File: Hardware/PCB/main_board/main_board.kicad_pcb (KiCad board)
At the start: 2 copper layers, 150 x 160 mm, 99 parts, among them J1 SWD, J2 USB_A, J3 DIN-5_180degree, J4 USB_B, J5 Conn_Coaxial, J6 AudioJack3, Q1 BC547, U1 MCP6002-xSN, U2 NUCLEO-F446RE, U3 6N137, U4 RC4558

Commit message: Route PCB changes
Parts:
- added C33: 100n, Capacitor_SMD:C_0805_2012Metric, F.Cu at (108.8, 200.6)
- added C34: 100n, Capacitor_SMD:C_0805_2012Metric, F.Cu at (97.4, 107.5)
- added C35: 100n, Capacitor_SMD:C_0805_2012Metric, F.Cu at (94.0, 108.5)
- added C36: 47u, Capacitor_SMD:CP_Elec_6.3x5.4, F.Cu at (95.0, 100.0)
- added C37: 4.7u, Capacitor_SMD:C_0805_2012Metric, F.Cu at (85.0, 110.4)
- added C38: 150p, Capacitor_SMD:C_0805_2012Metric, F.Cu at (86.5, 114.0)
- added C39: 47u, Capacitor_SMD:CP_Elec_6.3x5.4, F.Cu at (95.0, 92.5)
- added Q2: BC847B, Package_TO_SOT_SMD:SOT-23, F.Cu at (84.0, 100.5)
- added Q3: BC847B, Package_TO_SOT_SMD:SOT-23, F.Cu at (88.0, 96.5)
- added Q4: BC857B, Package_TO_SOT_SMD:SOT-23, F.Cu at (88.0, 100.5)
- added Q5: BC847B, Package_TO_SOT_SMD:SOT-23, F.Cu at (89.0, 204.0)
- added R20: 3.9k, Resistor_SMD:R_0805_2012Metric, F.Cu at (104.4, 203.5)
- added R21: 10k, Resistor_SMD:R_0805_2012Metric, F.Cu at (108.1, 203.5)
- added R22: 22M, Resistor_SMD:R_0805_2012Metric, F.Cu at (97.4, 105.5)
- added R23: 10k, Resistor_SMD:R_0805_2012Metric, F.Cu at (97.4, 111.5)
- added R24: 10M, Resistor_SMD:R_0805_2012Metric, F.Cu at (97.4, 109.5)
- added R25: 10k, Resistor_SMD:R_0805_2012Metric, F.Cu at (97.4, 113.5)
- added R26: 1k, Resistor_SMD:R_0805_2012Metric, F.Cu at (94.0, 112.0)
- added R27: 33, Resistor_SMD:R_0805_2012Metric, F.Cu at (85.0, 106.6)
- added R28: 10k, Resistor_SMD:R_0805_2012Metric, F.Cu at (84.0, 93.0)
- added R29: 10k, Resistor_SMD:R_0805_2012Metric, F.Cu at (88.0, 103.5)
- added R30: 56k, Resistor_SMD:R_0805_2012Metric, F.Cu at (90.0, 114.0)
- added R31: 10k, Resistor_SMD:R_0805_2012Metric, F.Cu at (87.5, 89.0)
- added R32: 100, Resistor_SMD:R_0805_2012Metric, F.Cu at (87.5, 93.0)
- added R33: 100, Resistor_SMD:R_0805_2012Metric, F.Cu at (87.5, 91.0)
- added U5: MCP6002-xSN, Package_SO:SOIC-8_3.9x4.9mm_P1.27mm, F.Cu at (90.0, 108.5)
- Q1: value BC547 -> BC857B; footprint Package_TO_SOT_THT:TO-92_Inline -> Package_TO_SOT_SMD:SOT-23
- RV_VOL1: value R_POT_Dual -> 500k reverse log; footprint Potentiometer_THT:Potentiometer_Alps_RK09L_Double_Vertical -> Potentiometer_THT:Potentiometer_Alps_RK09K_Single_Vertical
- moved Q1 106.6 mm to (84.0, 96.5), turned to 180 degrees
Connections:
- C16 pad 2: /analogFX/OUT_VCF__IN_DIST -> /analogFX/IN_DIST
- C4 pad 1: /analogFX/OUT_VCF__IN_DIST -> /analogFX/OUT_VCF
- Q1 pad 1: Net-(C2-Pad1) -> Net-(Q1-Pad1)
- R1 pad 1: Net-(Q1-Pad2) -> Net-(Q5-Pad1)
- R19 pad 2: /analogFX/AUDIO_OUT -> /audio_out/AUDIO_IN
- R2 pad 1: Net-(Q1-Pad2) -> Net-(Q5-Pad1)
- R5 pad 1: Net-(R5-Pad1) -> /analogFX/2.5V_midpoint
- R6 pad 1: Net-(R5-Pad1) -> /analogFX/2.5V_midpoint
- RV_VOL1 pad 1: Net-(RV_VOL1-Pad1) -> Net-(C38-Pad2)
- RV_VOL1 pad 2: Net-(RV_VOL1-Pad2) -> Net-(C38-Pad2)
- U1 pad 3: Net-(R5-Pad1) -> /analogFX/2.5V_midpoint
- U1 pad 5: GND -> /analogFX/2.5V_midpoint
- U1 pad 6: Net-(U1-Pad6) -> Net-(R20-Pad1)
- U1 pad 7: Net-(U1-Pad6) -> Net-(C33-Pad2)
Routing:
- net +5VA: track 250.0 -> 356.7 mm, vias 0 -> 6
- net Net-(J6-PadR): track 5.50 -> 106.6 mm, vias 0 -> 2
- net /audio_out/AUDIO_IN: track 0.00 -> 99.0 mm, vias 0 -> 4
- net Net-(C38-Pad2): track 0.00 -> 46.3 mm, vias 0 -> 2
- net Net-(C38-Pad1): track 0.00 -> 42.1 mm, vias 0 -> 2
- net Net-(R27-Pad2): track 0.00 -> 38.1 mm, vias 0 -> 2
- net /analogFX/OUT_VCF__IN_DIST: track 34.2 -> 0.00 mm, vias 2 -> 0
- net GND: track 74.7 -> 107.3 mm, vias 10 -> 16
- net /analogFX/IN_DIST: track 0.00 -> 25.4 mm, vias 0 -> 2
- net Net-(C33-Pad2): track 0.00 -> 23.1 mm, vias 0 -> 2
- net Net-(Q5-Pad1): track 0.00 -> 20.6 mm
- net Net-(R20-Pad1): track 0.00 -> 20.5 mm, vias 0 -> 2
- net Net-(Q1-Pad1): track 0.00 -> 16.9 mm
- net Net-(Q1-Pad2): track 21.7 -> 7.08 mm
- net Net-(C36-Pad1): track 0.00 -> 14.3 mm
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
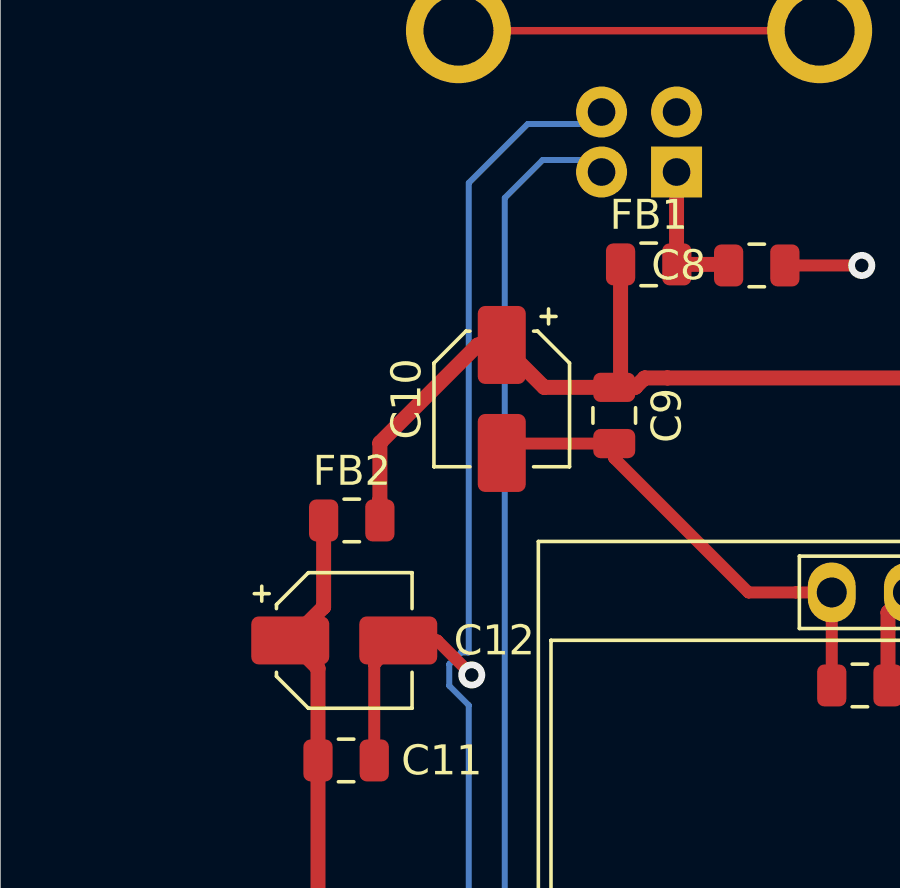
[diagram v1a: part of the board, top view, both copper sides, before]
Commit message: Fix GND via
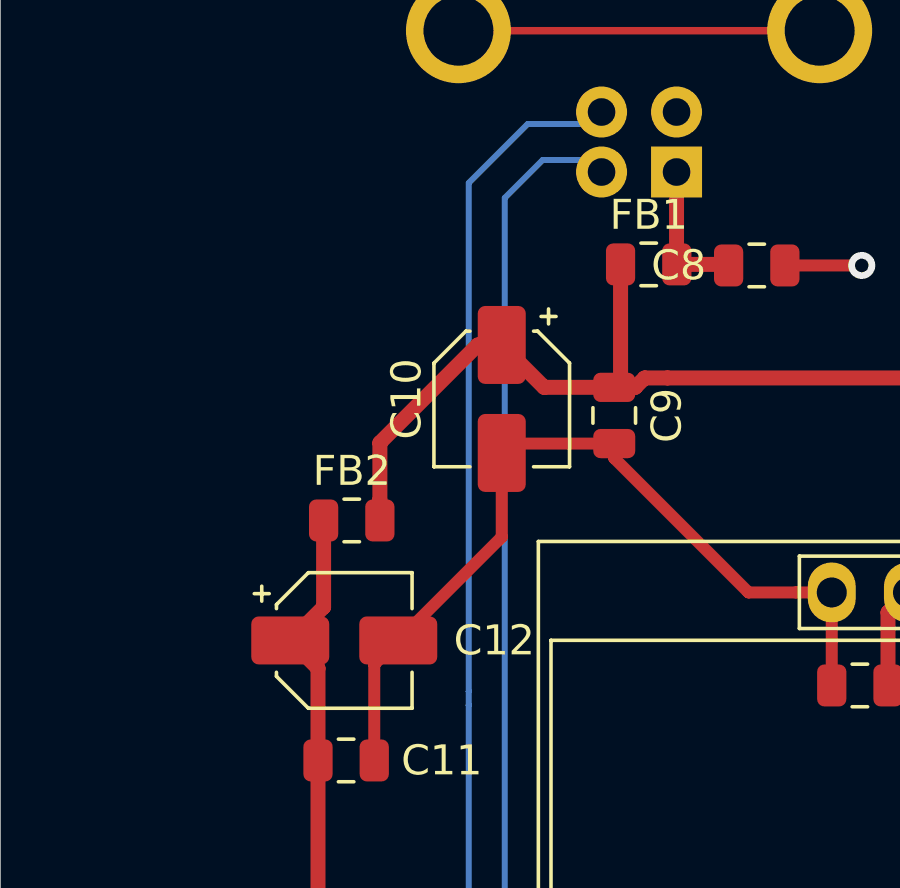
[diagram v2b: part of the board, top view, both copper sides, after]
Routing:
- net GND: track 107.3 -> 112.1 mm, vias 16 -> 15
- net /power/USB_B_D+: track 152.9 -> 152.2 mm
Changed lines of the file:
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@@
     (thickness 1.6)
     (drawings 3)
-    (tracks 945)
+    (tracks 942)
     (zones 0)
     (modules 125)
@@
   )
   (setup
-    (last_trace_width 0.5)
+    (last_trace_width 0.25)
     (user_trace_width 0.5)
     (trace_clearance 0.2)
@@
   (segment (start 85.85 95.55) (end 85.7 95.55) (width 0.25) (layer F.Cu) (net 6))
   (segment (start 87.1 97.5) (end 87.1 96.8) (width 0.25) (layer F.Cu) (net 6))
-  (segment (start 99.912 207.4835) (end 99.912 209.1645) (width 0.25) (layer F.Cu) (net 135))
   (segment (start 97.88 208.4025) (end 97.88 207.054) (width 0.4) (layer F.Cu) (net 7))
   (segment (start 110.983 79.386) (end 110.683 79.086) (width 0.4) (layer F.Cu) (net 7))
@@
   (segment (start 47.5 91.55) (end 48.3 90.75) (width 0.4) (layer F.Cu) (net 7))
   (segment (start 47.5 94.75) (end 47.5 91.55) (width 0.4) (layer F.Cu) (net 7))
-  (segment (start 49.6 90.75) (end 50.75 91.9) (width 0.4) (layer F.Cu) (net 7))
-  (segment (start 48.3 90.75) (end 49.6 90.75) (width 0.4) (layer F.Cu) (net 7))
-  (segment (start 50.75 91.9) (end 50.75 91.9) (width 0.4) (layer F.Cu) (net 7))
-  (via (at 50.75 91.9) (size 0.9) (drill 0.45) (layers F.Cu B.Cu) (net 7))
   (segment (start 89.75 74.0575) (end 87.3075 76.5) (width 0.4) (layer F.Cu) (net 7))
   (segment (start 89.75 72.96) (end 89.75 74.0575) (width 0.4) (layer F.Cu) (net 7))
@@
   (via (at 87 87.5) (size 0.9) (drill 0.45) (layers F.Cu B.Cu) (net 7))
   (segment (start 86.5625 87.9375) (end 87 87.5) (width 0.4) (layer F.Cu) (net 7))
+  (segment (start 51.75 87.3) (end 48.3 90.75) (width 0.4) (layer F.Cu) (net 7))
+  (segment (start 51.75 84.5) (end 51.75 87.3) (width 0.4) (layer F.Cu) (net 7))
   (segment (start 99.426473 211.525027) (end 99.912 211.0395) (width 0.25) (layer F.Cu) (net 8))
   (segment (start 92.7015 218.25) (end 99.426473 211.525027) (width 0.25) (layer F.Cu) (net 8))
   (segment (start 55.25 214.75) (end 58.75 218.25) (width 0.25) (layer F.Cu) (net 8))
   (segment (start 58.75 218.25) (end 92.7015 218.25) (width 0.25) (layer F.Cu) (net 8))
-  (segment (start 90.26 212.8175) (end 90.26 214.8495) (width 0.25) (layer F.Cu) (net 129))
-  (segment (start 90.26 214.8495) (end 90.3385 214.928) (width 0.25) (layer F.Cu) (net 129))
   (segment (start 93.837 214.928) (end 92.701 214.928) (width 0.5) (layer F.Cu) (net 9))
   (segment (start 92.701 214.928) (end 92.2135 214.928) (width 0.5) (layer F.Cu) (net 9))
@@
   (segment (start 84.5 88) (end 86 86.5) (width 0.5) (layer F.Cu) (net 81))
   (segment (start 86 86.5) (end 102.5 86.5) (width 0.5) (layer F.Cu) (net 81))
-  (segment (start 50.65 91.149999) (end 50.389999 91.149999) (width 0.2) (layer B.Cu) (net 82))
-  (segment (start 50.65 75.50147) (end 50.65 91.149999) (width 0.2) (layer B.Cu) (net 82))
-  (segment (start 55.077 73.135) (end 54.677 73.535) (width 0.2) (layer B.Cu) (net 82))
-  (segment (start 50.389999 91.149999) (end 49.999999 91.539999) (width 0.2) (layer B.Cu) (net 82))
+  (segment (start 111.48853 158.11) (end 111.83 158.11) (width 0.2) (layer F.Cu) (net 82))
+  (segment (start 111.83 158.11) (end 112.5 158.78) (width 0.2) (layer F.Cu) (net 82))
+  (segment (start 93.75 164.9) (end 94.05 164.6) (width 0.2) (layer F.Cu) (net 82))
+  (segment (start 104.99853 164.6) (end 111.48853 158.11) (width 0.2) (layer F.Cu) (net 82))
+  (segment (start 94.05 164.6) (end 104.99853 164.6) (width 0.2) (layer F.Cu) (net 82))
   (via (at 93.75 164.9) (size 0.8) (drill 0.4) (layers F.Cu B.Cu) (net 82))
+  (segment (start 93.45 164.6) (end 93.75 164.9) (width 0.2) (layer B.Cu) (net 82))
+  (segment (start 63.25147 164.6) (end 93.45 164.6) (width 0.2) (layer B.Cu) (net 82))
+  (segment (start 50.65 75.50147) (end 50.65 92.446806) (width 0.2) (layer B.Cu) (net 82))
+  (segment (start 50.65 92.446806) (end 50.649321 92.447485) (width 0.2) (layer B.Cu) (net 82))
+  (segment (start 52.61647 73.535) (end 50.65 75.50147) (width 0.2) (layer B.Cu) (net 82))
+  (segment (start 50.65 112.74853) (end 54.65 116.74853) (width 0.2) (layer B.Cu) (net 82))
+  (segment (start 55.077 73.135) (end 54.677 73.535) (width 0.2) (layer B.Cu) (net 82))
   (segment (start 54.677 73.535) (end 52.61647 73.535) (width 0.2) (layer B.Cu) (net 82))
-  (segment (start 49.999999 92.260001) (end 50.65 92.910002) (width 0.2) (layer B.Cu) (net 82))
+  (segment (start 50.649321 92.447485) (end 50.649321 92.909323) (width 0.2) (layer B.Cu) (net 82))
   (segment (start 54.65 116.74853) (end 54.65 155.99853) (width 0.2) (layer B.Cu) (net 82))
+  (segment (start 50.649321 92.909323) (end 50.65 92.910002) (width 0.2) (layer B.Cu) (net 82))
   (segment (start 50.65 92.910002) (end 50.65 112.74853) (width 0.2) (layer B.Cu) (net 82))
-  (segment (start 49.999999 91.539999) (end 49.999999 92.260001) (width 0.2) (layer B.Cu) (net 82))
-  (segment (start 52.61647 73.535) (end 50.65 75.50147) (width 0.2) (layer B.Cu) (net 82))
-  (segment (start 50.65 112.74853) (end 54.65 116.74853) (width 0.2) (layer B.Cu) (net 82))
   (segment (start 54.65 155.99853) (end 63.25147 164.6) (width 0.2) (layer B.Cu) (net 82))
-  (segment (start 63.25147 164.6) (end 93.45 164.6) (width 0.2) (layer B.Cu) (net 82))
-  (segment (start 93.45 164.6) (end 93.75 164.9) (width 0.2) (layer B.Cu) (net 82))
-  (segment (start 93.75 164.9) (end 94.05 164.6) (width 0.2) (layer F.Cu) (net 82))
-  (segment (start 94.05 164.6) (end 104.99853 164.6) (width 0.2) (layer F.Cu) (net 82))
-  (segment (start 111.48853 158.11) (end 111.83 158.11) (width 0.2) (layer F.Cu) (net 82))
-  (segment (start 111.83 158.11) (end 112.5 158.78) (width 0.2) (layer F.Cu) (net 82))
-  (segment (start 104.99853 164.6) (end 111.48853 158.11) (width 0.2) (layer F.Cu) (net 82))
   (segment (start 93.45 163.4) (end 93.75 163.1) (width 0.2) (layer B.Cu) (net 83))
   (segment (start 63.74853 163.4) (end 93.45 163.4) (width 0.2) (layer B.Cu) (net 83))
@@
   (segment (start 46.375 124.25) (end 45 122.875) (width 0.25) (layer B.Cu) (net 101))
   (segment (start 48.25 124.25) (end 46.375 124.25) (width 0.25) (layer B.Cu) (net 101))
-  (segment (start 98.75 185.0625) (end 100.8125 183) (width 0.25) (layer F.Cu) (net 119))
-  (segment (start 100.8125 183) (end 104.75 183) (width 0.25) (layer F.Cu) (net 119))
-  (segment (start 104.75 183) (end 109 187.25) (width 0.25) (layer F.Cu) (net 119))
-  (segment (start 109 187.25) (end 109 190.25) (width 0.25) (layer F.Cu) (net 119))
-  (segment (start 109 190.25) (end 109 190.25) (width 0.25) (layer F.Cu) (net 119))
   (segment (start 100.8125 188.5) (end 100.8125 186.25) (width 0.25) (layer F.Cu) (net 102))
   (segment (start 98.1775 191.885) (end 98.75 191.3125) (width 0.25) (layer F.Cu) (net 103))
@@
   (segment (start 103.498 203.498) (end 103.5 203.5) (width 0.25) (layer F.Cu) (net 118))
   (segment (start 100.0875 203.498) (end 103.498 203.498) (width 0.25) (layer F.Cu) (net 118))
+  (segment (start 98.75 185.0625) (end 100.8125 183) (width 0.25) (layer F.Cu) (net 119))
+  (segment (start 100.8125 183) (end 104.75 183) (width 0.25) (layer F.Cu) (net 119))
+  (segment (start 104.75 183) (end 109 187.25) (width 0.25) (layer F.Cu) (net 119))
+  (segment (start 109 187.25) (end 109 190.25) (width 0.25) (layer F.Cu) (net 119))
+  (segment (start 109 190.25) (end 109 190.25) (width 0.25) (layer F.Cu) (net 119))
   (segment (start 109 198) (end 109 197) (width 0.25) (layer B.Cu) (net 119))
   (via (at 109 198) (size 0.8) (drill 0.4) (layers F.Cu B.Cu) (net 119))
@@
   (segment (start 87.0625 101.5125) (end 87.05 101.5) (width 0.25) (layer F.Cu) (net 128))
   (segment (start 87.0625 103.5) (end 87.0625 101.5125) (width 0.25) (layer F.Cu) (net 128))
+  (segment (start 90.26 212.8175) (end 90.26 214.8495) (width 0.25) (layer F.Cu) (net 129))
+  (segment (start 90.26 214.8495) (end 90.3385 214.928) (width 0.25) (layer F.Cu) (net 129))
   (segment (start 93.435 206.865) (end 93.435 209.065) (width 0.25) (layer F.Cu) (net 129))
   (segment (start 92.165 210.335) (end 92.165 211.815) (width 0.25) (layer F.Cu) (net 129))
@@
   (segment (start 86.6 105.1) (end 83.05 101.55) (width 0.25) (layer F.Cu) (net 134))
   (segment (start 88.095 109.795) (end 86.6 108.3) (width 0.25) (layer F.Cu) (net 134))
+  (segment (start 99.912 207.4835) (end 99.912 209.1645) (width 0.25) (layer F.Cu) (net 135))
   (segment (start 98.69184 204.71816) (end 98.69184 206.26334) (width 0.25) (layer F.Cu) (net 135))
   (segment (start 91.304 200.196) (end 98.671425 200.196) (width 0.25) (layer F.Cu) (net 135))

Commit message: Fix DRC issue
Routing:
- net /analogFX/CV_IN: track 45.2 -> 46.0 mm
